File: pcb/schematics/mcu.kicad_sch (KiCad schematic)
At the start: 25 parts, among them J3 Conn_01x06_Female, SW2 Reset, U3 STM32F103V8Tx, Y2 24MHz

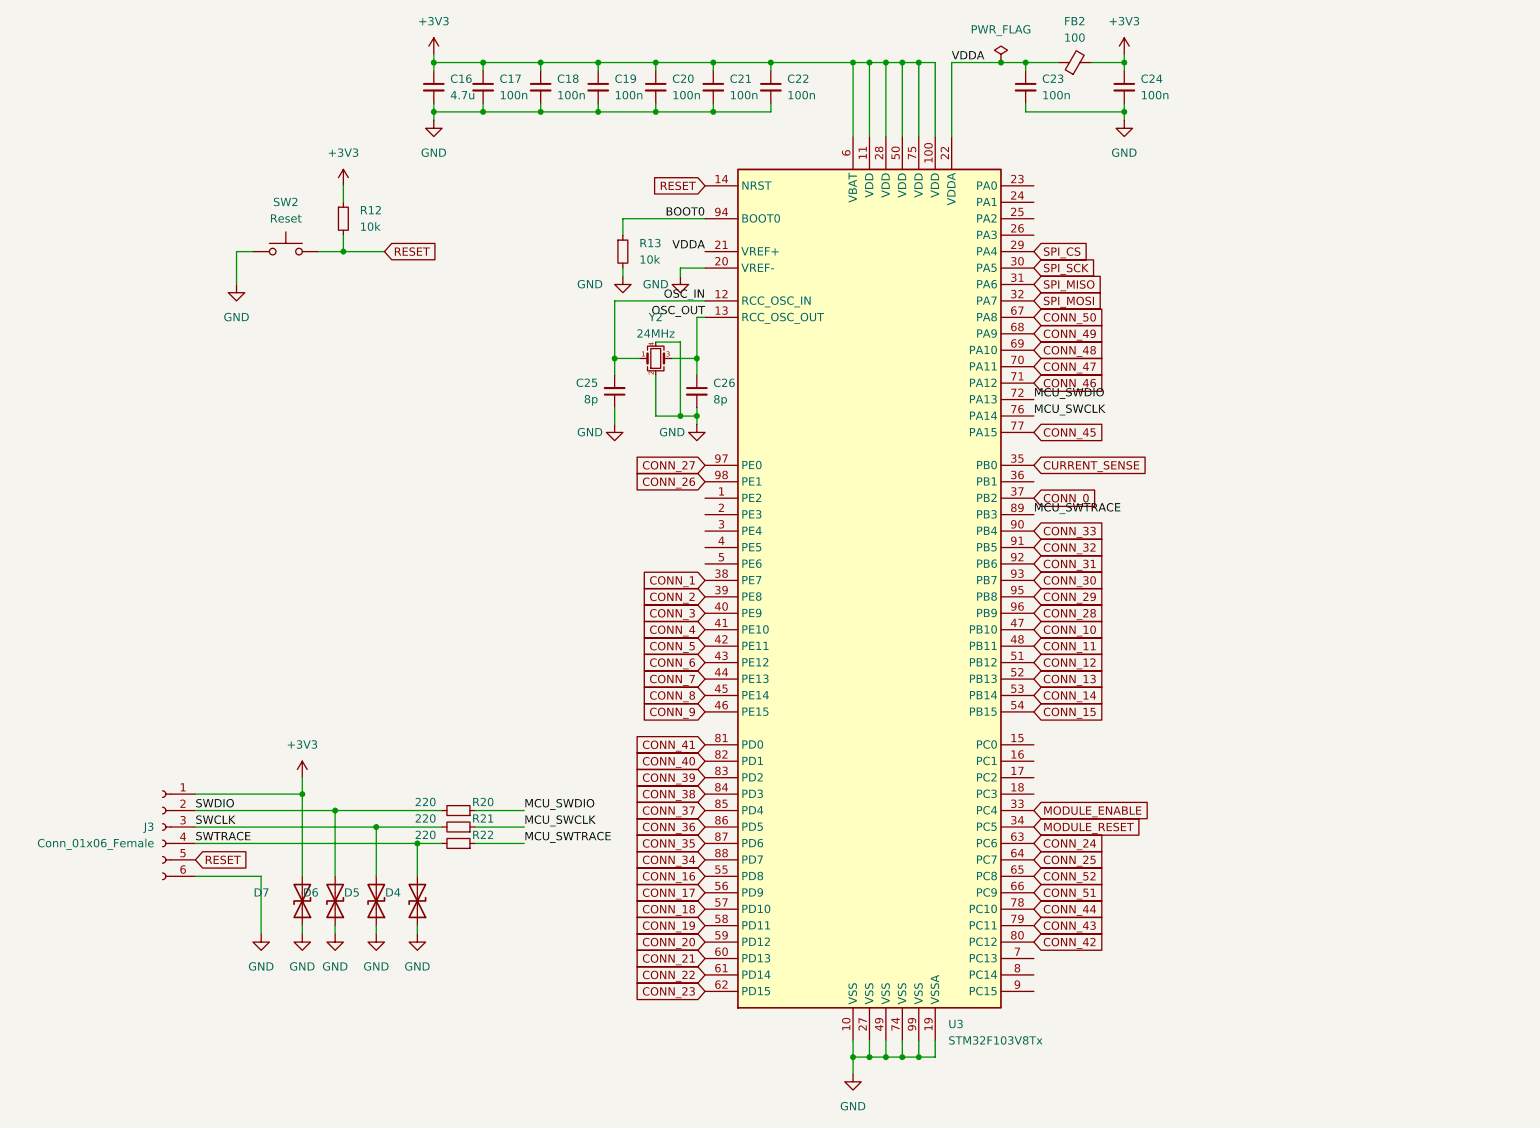
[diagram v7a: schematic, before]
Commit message: finished routing the bus traces
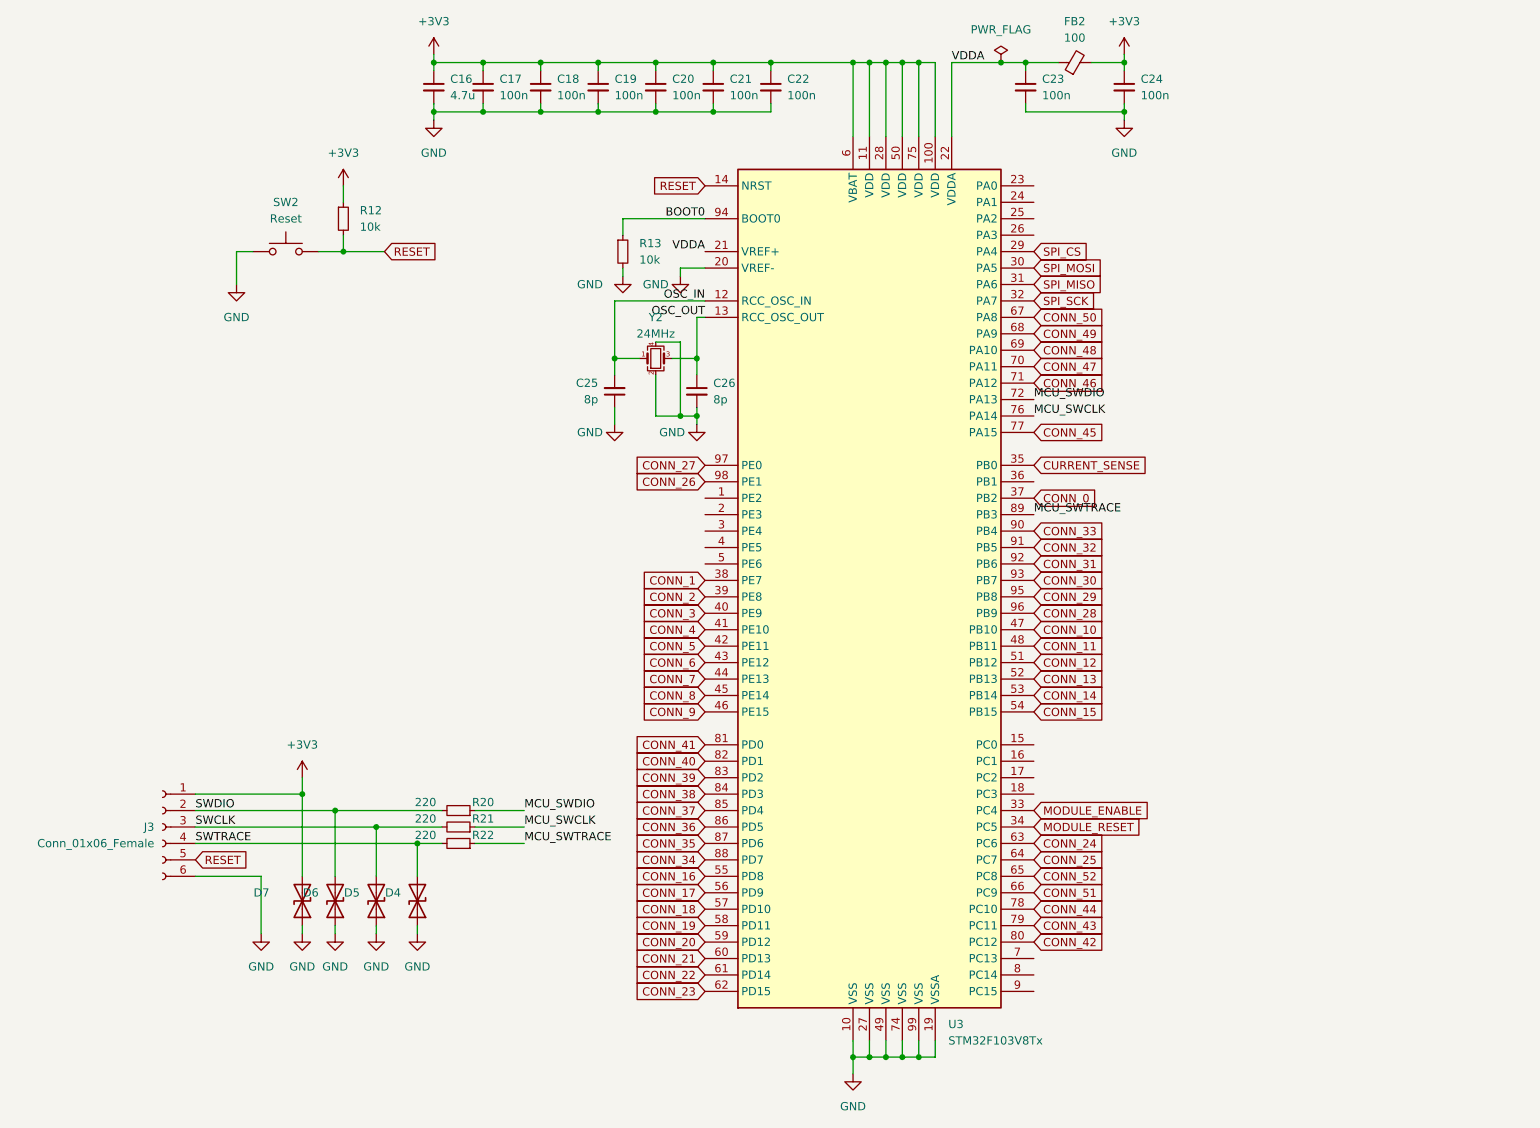
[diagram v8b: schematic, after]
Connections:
- net SPI_MOSI: now also U3.30 (PA5); no longer U3.32 (PA7)
- net SPI_SCK: now also U3.32 (PA7); no longer U3.30 (PA5)
